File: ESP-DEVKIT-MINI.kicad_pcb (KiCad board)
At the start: 2 copper layers, 43.2 x 83.8 mm, 41 parts, among them J1 Conn_01x22_Pin, J2 Conn_01x22_Pin, J3 USB_C_Receptacle_USB2.0, J4 USB_B_Mini, J5 USB_B_Micro, Q1 L8050QLT1G, Q2 L8050QLT1G, SW1 SW_Omron_B3FS, SW2 SW_Omron_B3FS, U1 ESP32-S3-MINI-1-N8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

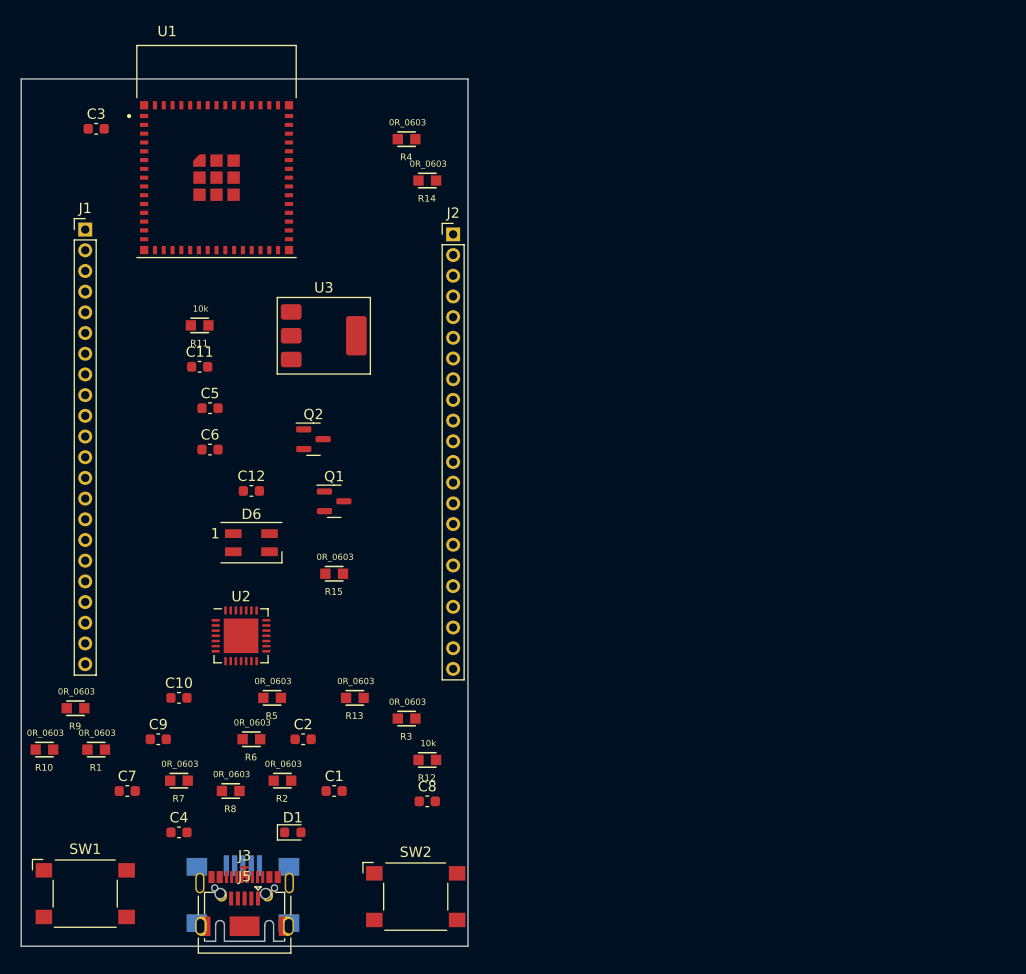
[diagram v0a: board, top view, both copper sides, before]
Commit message: Final 1.0
The PCB routing is finished, and the Silscreen is only to be changed.
For the BOM the schematic must be used due to the reuse of similar components
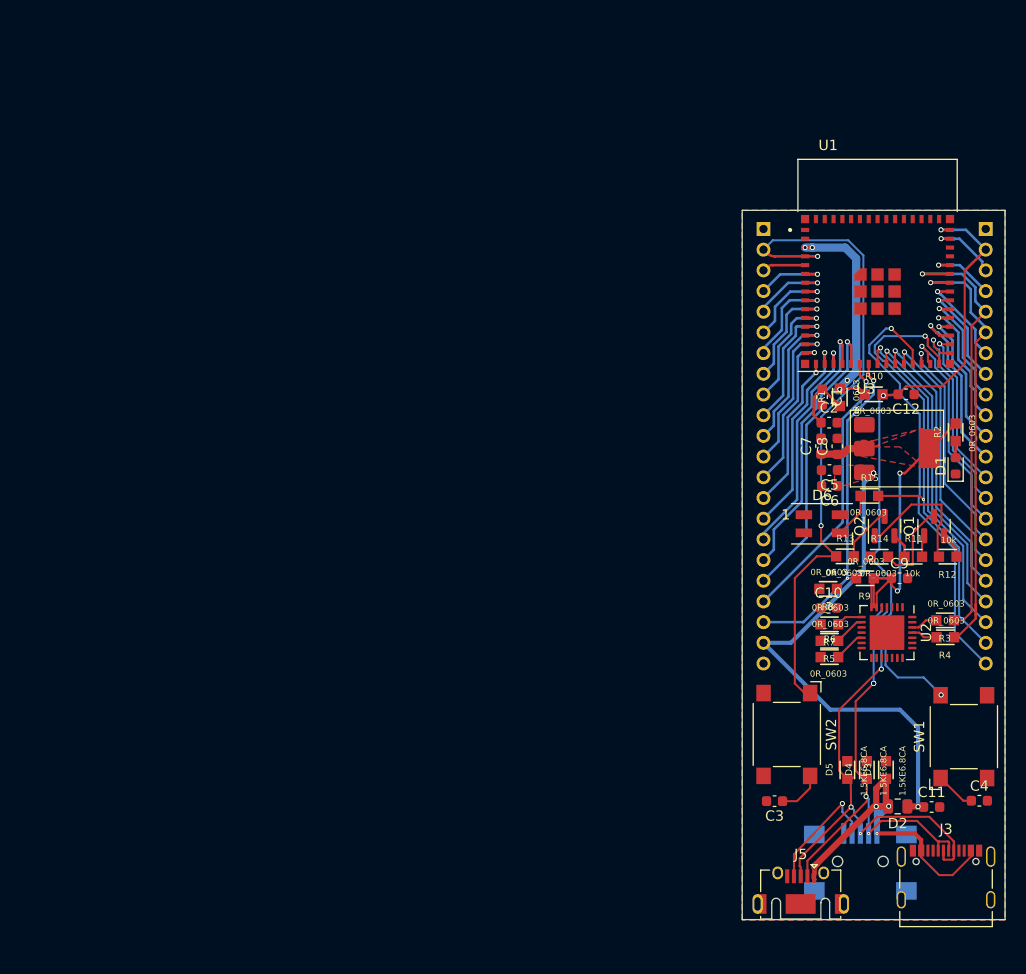
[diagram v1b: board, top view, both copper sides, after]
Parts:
- added D2: 1N5819HW-7-F, PCM_4ms_Resistor:R_0805_2012Metric, F.Cu at (106.5, 113.5)
- added D3: 1.5KE6.8CA, PCM_4ms_Resistor:R_0603, F.Cu at (105.3, 110.0)
- added D4: 1.5KE6.8CA, PCM_4ms_Resistor:R_0603, F.Cu at (103.5, 110.0)
- added D5: 1.5KE6.8CA, PCM_4ms_Resistor:R_0603, F.Cu at (101.6, 110.0)
- J1, J2: moved to B.Cu
- moved C3 92.3 mm to (94.6, 113.0), turned to 180 degrees
- moved R10 87.2 mm to (104.1, 73.7), turned to 180 degrees
- moved SW1 86.3 mm to (112.9, 106.7), turned to 90 degrees
- moved C11 82.6 mm to (109.7, 113.6)
- moved R1 79.5 mm to (100.9, 73.9), turned to -90 degrees
- moved C4 77.4 mm to (114.4, 112.9)
- moved R9 77.3 mm to (103.3, 91.4)
- moved C7 74.9 mm to (99.1, 78.7), turned to 90 degrees
- moved C9 73.3 mm to (106.6, 91.4)
- moved R2 73.3 mm to (112.1, 77.3), turned to -90 degrees
- moved D1 73.2 mm to (112.1, 80.6), turned to 90 degrees
- moved R11 72.5 mm to (108.0, 89.4), turned to 180 degrees
- moved R4 70.9 mm to (111.1, 97.1)
- moved J3 67.8 mm to (111.1, 120.3)
- moved J1 65.6 mm to (93.5, 57.7), turned to 180 degrees
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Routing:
- net GPIO0: track 0.00 -> 68.7 mm, vias 0 -> 2
- net CHIP_PU: track 0.00 -> 65.1 mm, vias 0 -> 4
- net VCC_5V: track 0.00 -> 49.9 mm, vias 0 -> 3
- net GPIO48: track 0.00 -> 46.4 mm, vias 0 -> 2
- net USB_DN: track 0.00 -> 45.4 mm, vias 0 -> 4
- net USB_DP: track 2.75 -> 48.0 mm, vias 0 -> 3
- net VCC_3V3: track 0.00 -> 44.2 mm, vias 0 -> 2
- net U0TXD: track 0.00 -> 42.8 mm, vias 0 -> 1
- net U0RXD: track 0.00 -> 42.6 mm, vias 0 -> 1
- net GPIO47: track 0.00 -> 42.6 mm, vias 0 -> 1
- net VBUS: track 0.00 -> 34.3 mm, vias 0 -> 3
- net GPIO18: track 0.00 -> 32.7 mm, vias 0 -> 2
- net GPIO19: track 0.00 -> 32.5 mm, vias 0 -> 1
- net GPIO20: track 0.00 -> 29.4 mm, vias 0 -> 1
- net GPIO16: track 0.00 -> 28.8 mm, vias 0 -> 1
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- added copper zone on B.Cu, net GND
- added copper zone on F.Cu, net GND
- added copper zone on F.Cu, net VBUS
- added copper zone on F.Cu, net VCC_3V3
- added copper zone on F.Cu, net VCC_5V
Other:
- board size 43.2 x 83.8 mm -> 25.4 x 68.6 mm
